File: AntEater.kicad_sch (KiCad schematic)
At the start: 30 parts, among them CN1 X2026WRS-2X09D-LPSW, CN2 X2026WRS-2X09D-LPSW, J1 USB_C_Receptacle_USB2.0, J3 Conn_02x06_Odd_Even, U1 W25X40CLUXIG TR, U2 AP2112K-3.3TRG1, U4 RP2040, Y1 12MHz

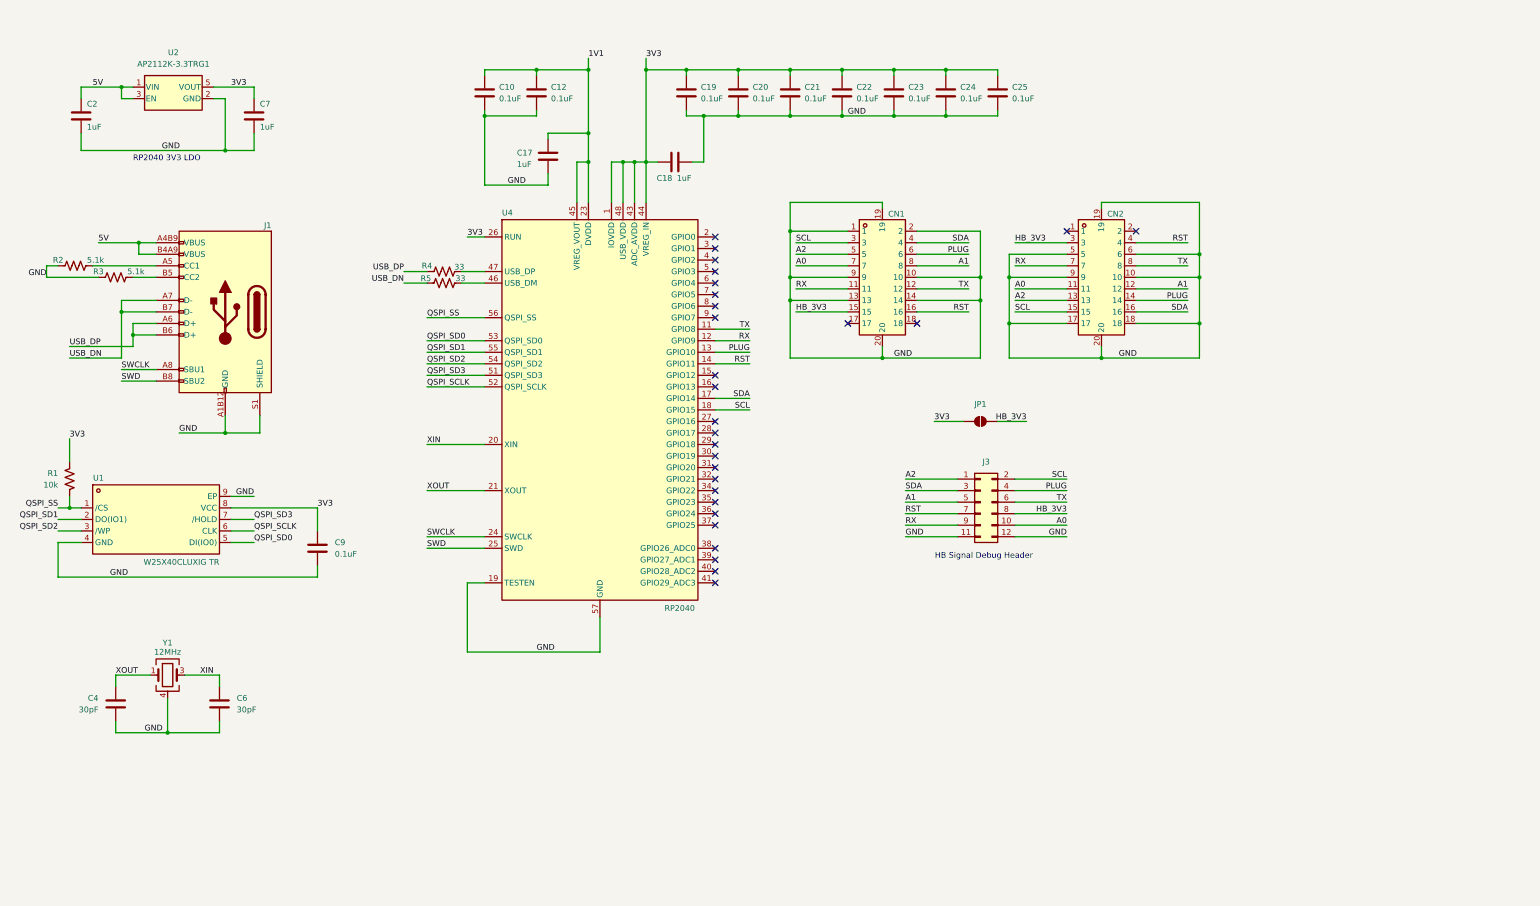
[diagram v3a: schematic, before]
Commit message: switched to RPi Pico
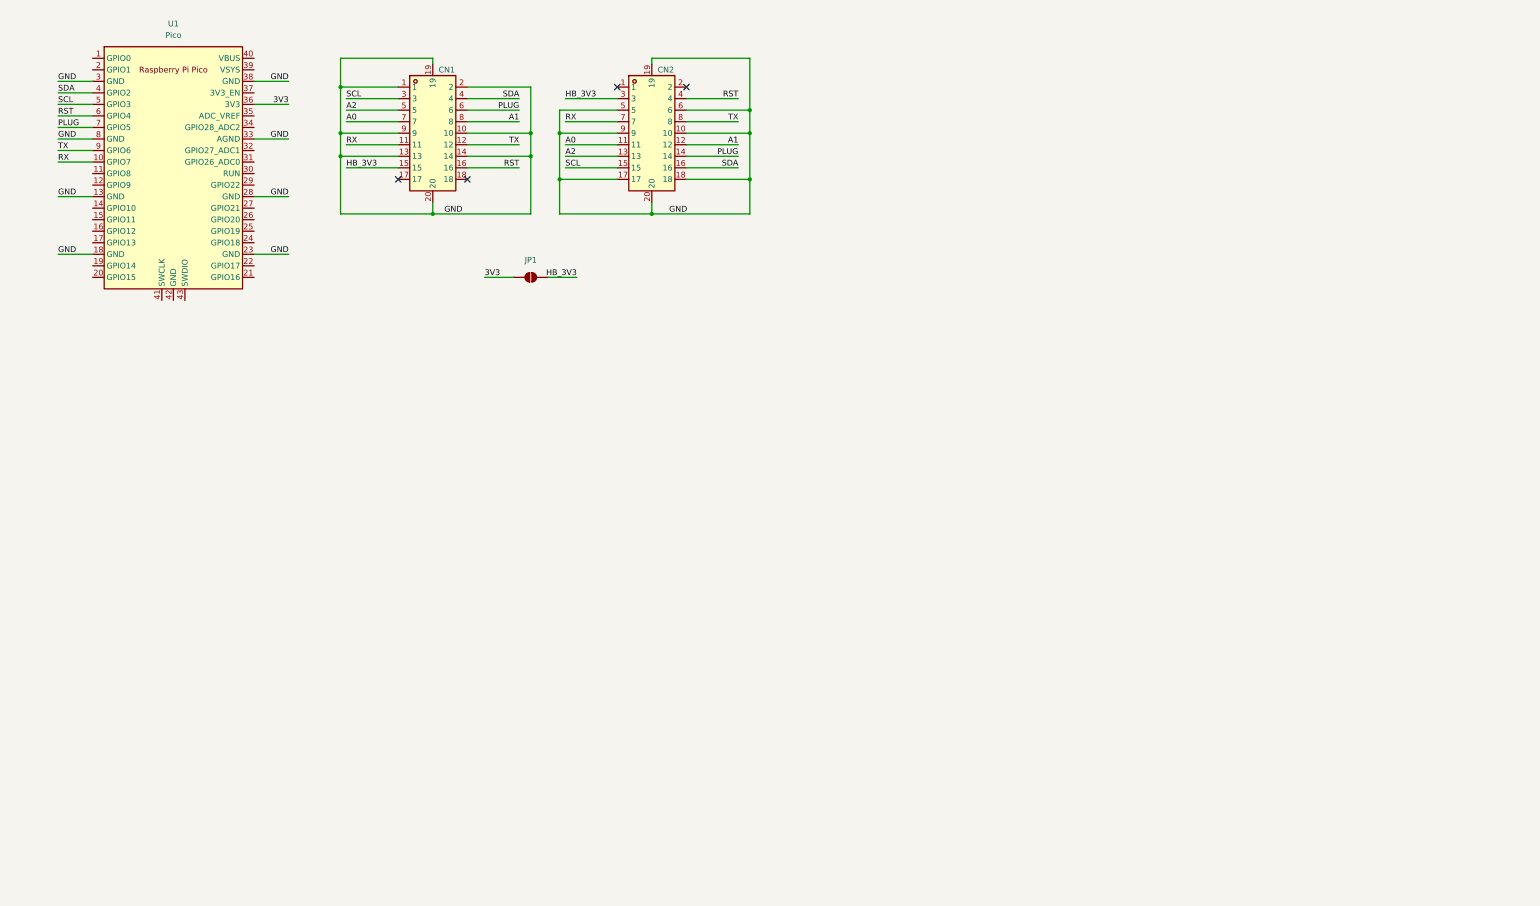
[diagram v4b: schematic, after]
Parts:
- removed C10, C12, C19, C20, C21, C22, C23, C24, C25, C9: 0.1uF, Capacitor_SMD:C_0402_1005Metric, symbol Device:C
- removed C17, C18, C2, C7: 1uF, Capacitor_SMD:C_0402_1005Metric, symbol Device:C
- removed C4, C6: 30pF, Capacitor_SMD:C_0402_1005Metric, symbol Device:C
- removed J1: USB_C_Receptacle_USB2.0, antsniffer:USB_C_Receptacle_GCT_USB4105-xx-A_16P_TopMnt_Horizontal, symbol antsniffer:USB_C_Receptacle_USB2.0
- removed J3: Conn_02x06_Odd_Even, Connector_PinHeader_2.54mm:PinHeader_2x06_P2.54mm_Vertical, symbol Connector_Generic:Conn_02x06_Odd_Even
- removed R1: 10k, Resistor_SMD:R_0402_1005Metric, symbol Device:R_US
- removed R2, R3: 5.1k, Resistor_SMD:R_0402_1005Metric, symbol Device:R_US
- removed R4, R5: 33, Resistor_SMD:R_0402_1005Metric, symbol Device:R_US
- removed U1: W25X40CLUXIG TR, antsniffer:USON8_L2.0-W3.0-P0.50-BL-EP, symbol antsniffer:W25X40CLUXIGTR
- removed U2: AP2112K-3.3TRG1, antsniffer:SOT-25-5_L2.9-W1.6-P0.95-LS2.8-BL, symbol antsniffer:AP2112K-3.3TRG1
- removed U4: RP2040, Package_DFN_QFN:QFN-56-1EP_7x7mm_P0.4mm_EP3.2x3.2mm, symbol aditBoard:RP2040
- removed Y1: 12MHz, antsniffer:OSC-SMD_4P-L3.2-W2.5-BL, symbol Device:Crystal_GND24_common
- added U1: Pico, antsniffer:RPi_Pico_SMD_TH, symbol antsniffer:Pico
- CN1, CN2: footprint antsniffer:CONN-SMD_X2026WRS-2X09D-LPSW -> antsniffer:CONN-TH_X2026WV-2-09D-46SN
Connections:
- net 3V3: now also U1.36 (3V3)
- net GND: now also U1.13 (GND), U1.18 (GND), U1.23 (GND), U1.28 (GND), U1.3 (GND), U1.33 (AGND), U1.38 (GND), U1.8 (GND)
- net PLUG: now also U1.7 (GPIO5)
- net RST: now also U1.6 (GPIO4)
- net RX: now also U1.10 (GPIO7)
- net SCL: now also U1.5 (GPIO3)
- net SDA: now also U1.4 (GPIO2)
- net TX: now also U1.9 (GPIO6)
- no-connect marks 28 -> 4
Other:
- note removed: "HB Signal Debug Header"
- note removed: "RP2040 3V3 LDO"
- moved on the sheet: CN1, CN2, JP1
